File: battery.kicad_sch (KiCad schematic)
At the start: 62 parts, among them J10 SOLAR, Q10 SI2308, Q11 CSD17577Q3A, Q7 CSD18512Q5B, Q8 CSD18512Q5B, Q9 SI2308, SW3 POWER/RESET, U8 BQ25798

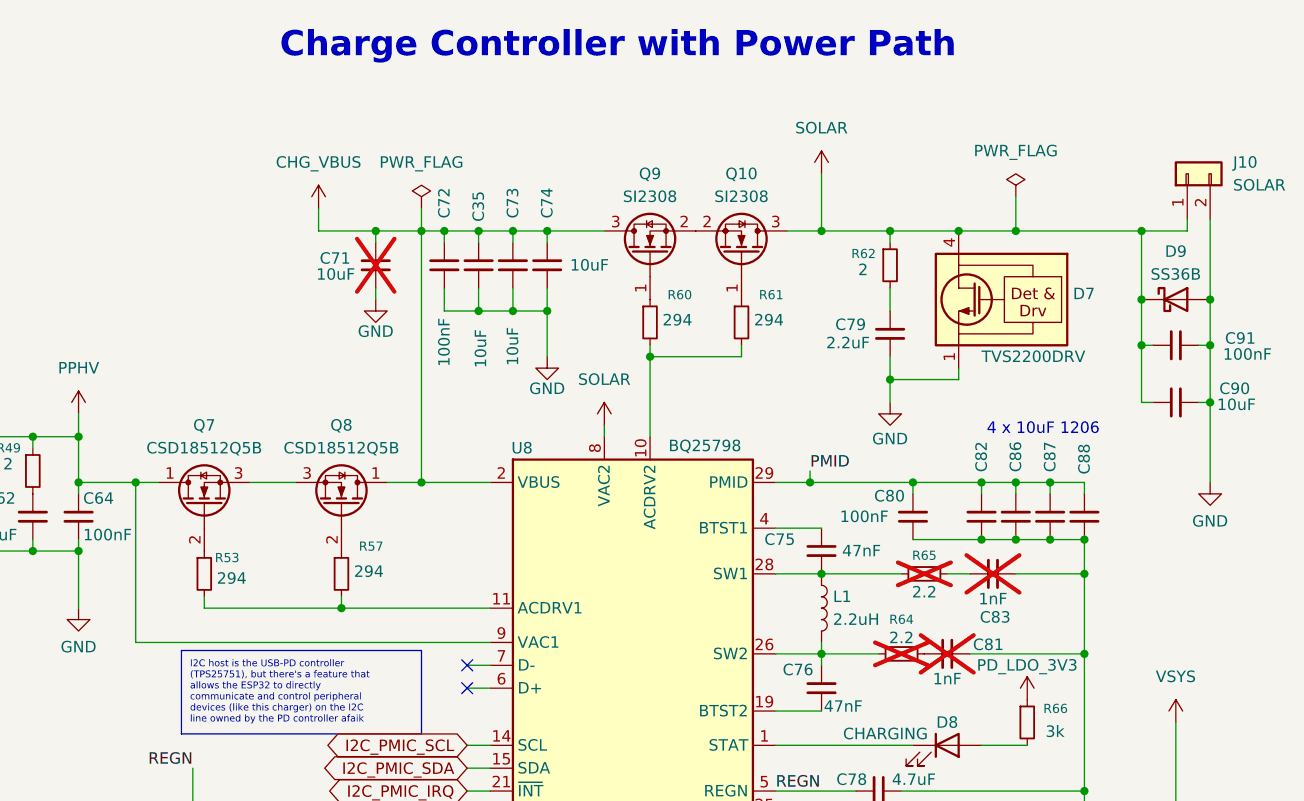
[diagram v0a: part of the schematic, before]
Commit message: schematic: add D24/D25 PZU12B2L zeners, Q_NMOS_SGD symbol, misc sheet edits
Co-Authored-By: Claude Opus 5.5 <noreply@anthropic.com>
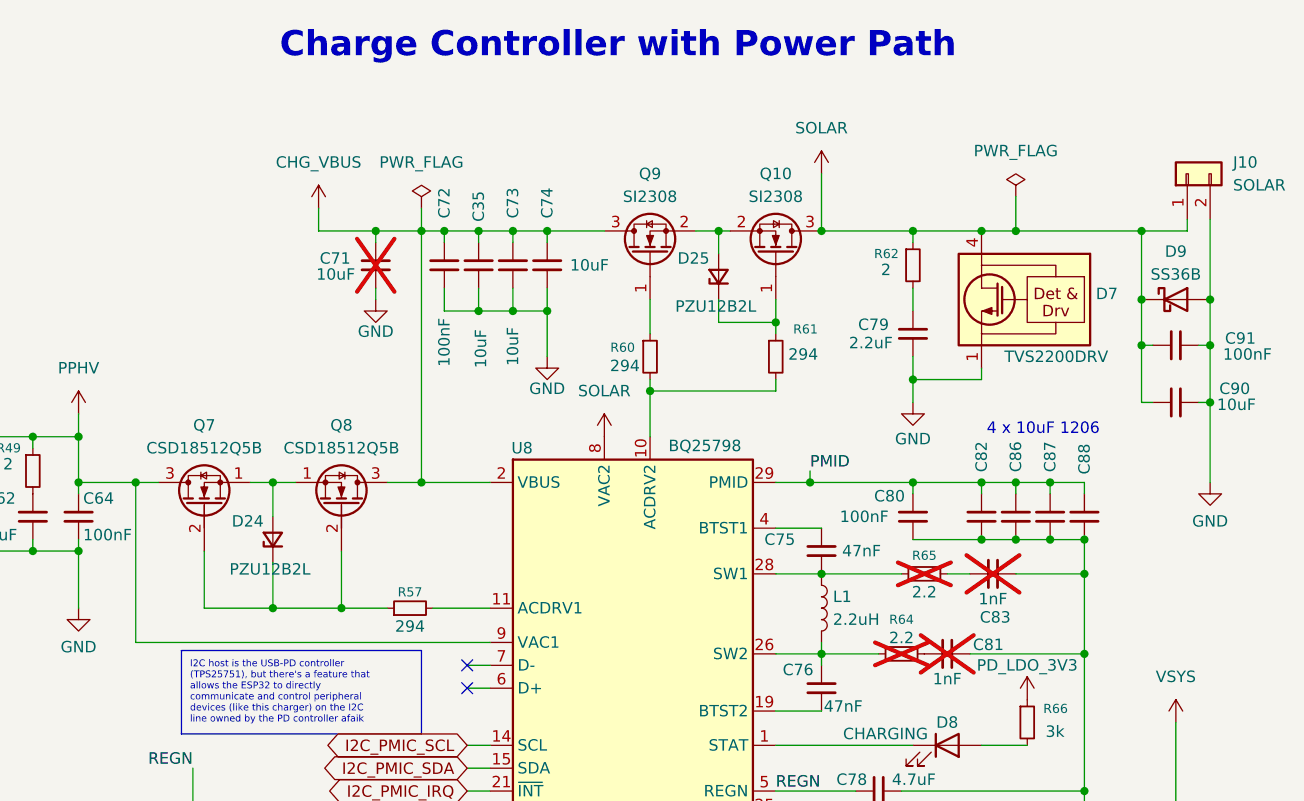
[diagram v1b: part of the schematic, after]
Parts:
- removed R53: 294, Resistor_SMD:R_0402_1005Metric, symbol Device:R_Small
- added D24, D25: PZU12B2L, Diode_SMD:D_SOD-882, symbol Device:D_Zener_Small
- Q7, Q8: symbol Transistor_FET:Q_NMOS_DGS -> Transistor_FET:Q_NMOS_SGD
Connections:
- net CHG_VBUS: now also Q8.3 (D); no longer Q8.1 (D)
- net PPHV: now also Q7.3 (D); no longer Q7.1 (D)
- net at Q8.2 (G), R57.1: now also Q7.2 (G), D24.1 (K)
- net at Q10.1 (G), R61.1: now also D25.1 (K)
- net at Q10.2 (S), Q9.2 (S): now also D25.2 (A)
- new net: D24.2 (A), Q7.1 (S), Q8.1 (S)
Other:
- moved on the sheet: C79, D7, Q10, R60, R61, R62

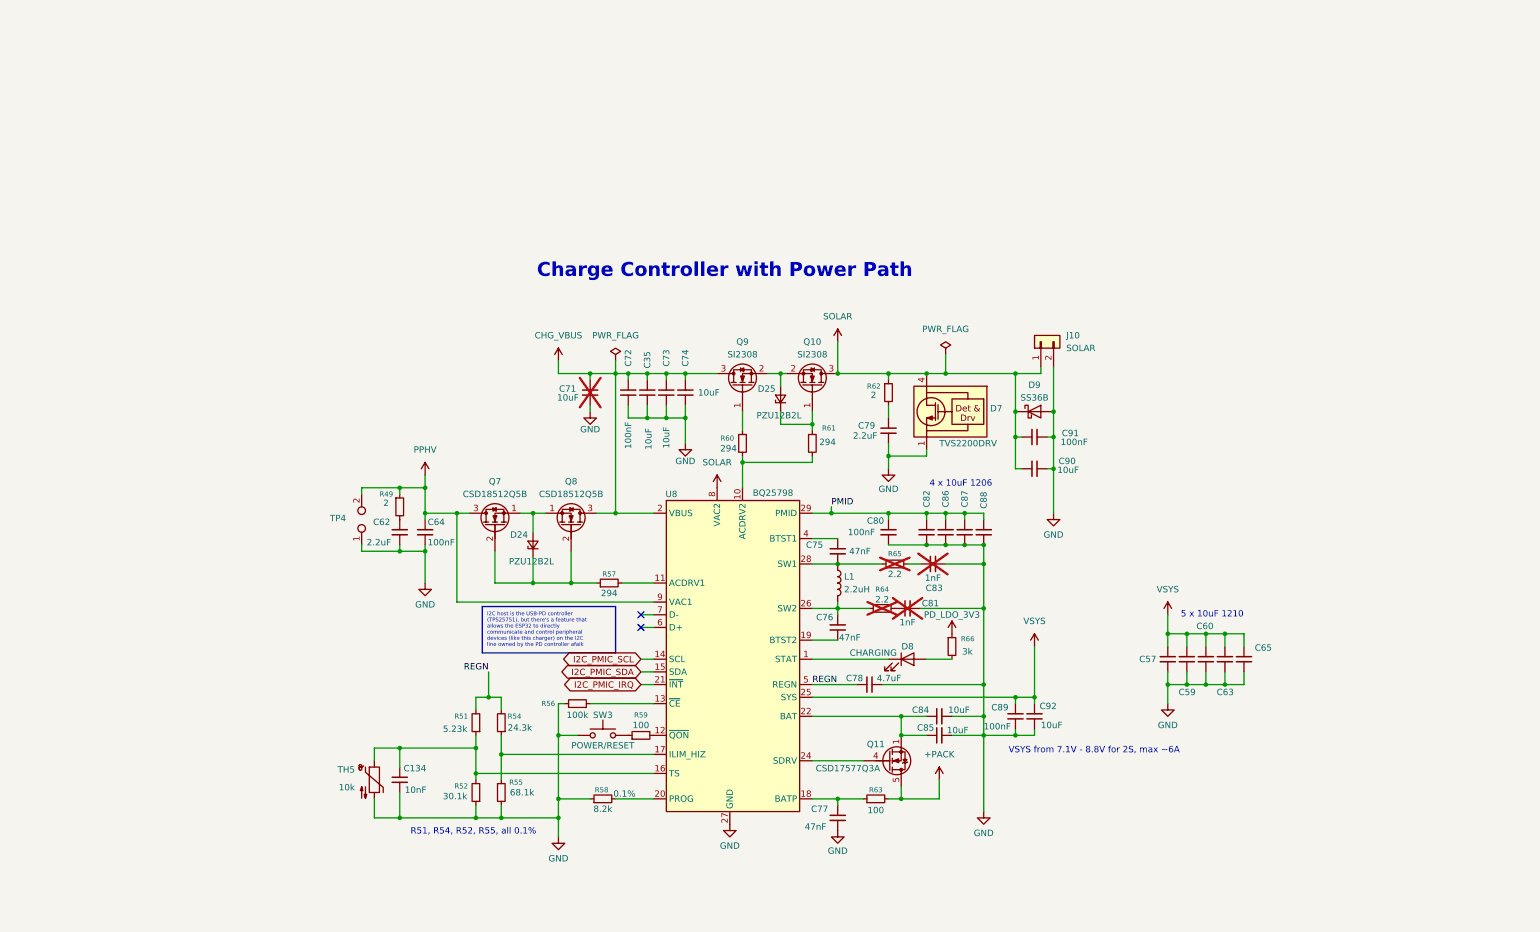
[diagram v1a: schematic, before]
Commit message: checkpoint: schematic WIP before battery -> charger rename
Connectors and Overview sheets, LSM6DSV16X/TPS22945/charger datasheets,
and in-progress edits across all sheets, committed as-is so the rename
diff stands alone.

Co-Authored-By: Claude Opus 5.5 <noreply@anthropic.com>
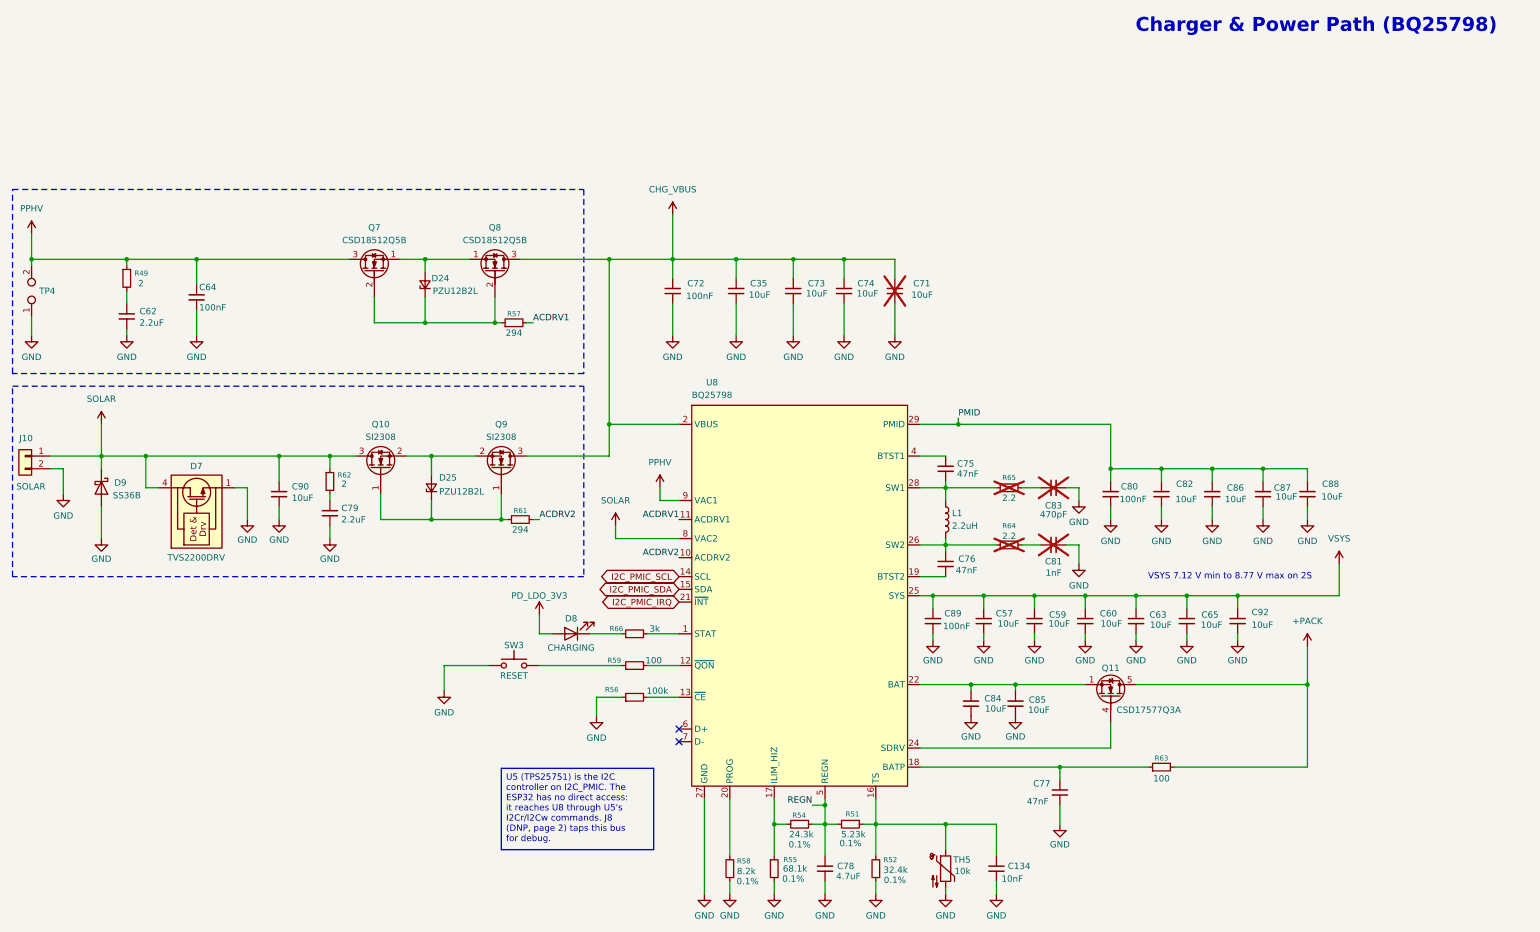
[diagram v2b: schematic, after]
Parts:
- removed C91: 100nF, Capacitor_SMD:C_0402_1005Metric, symbol Device:C_Small
- removed R60: 294, Resistor_SMD:R_0402_1005Metric, symbol Device:R_Small
- removed U8: BQ25798, Package_DFN_QFN:Texas_RQM0029A_VQFN-29_4x4mm_P0.4mm, symbol Battery_Management:BQ25798
- added U8: BQ25798, Package_DFN_QFN:Texas_RQM0029A_VQFN-29_4x4mm_P0.4mm, symbol parsnip-node:BQ25798
- C83: value 1nF -> 470pF
- L1: footprint Inductor_SMD:L_Sunlord_MWSA0503S -> Inductor_SMD:L_Sunlord_MWSA0603S; LCSC Part C408408 -> C357100; MPN MWSA0503S-2R2MT -> TMPA0603S-2R2MN-D
- R52: value 30.1k -> 32.4k; LCSC Part C2989442 -> C861323; MPN TC0325B3012T5F -> RT0603BRD0732K4L; Manufacturer UNI-ROYAL -> Yageo
- SW3: value POWER/RESET -> RESET
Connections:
- net CHG_VBUS: now also U8.2 (VBUS), U8.3 (VBUS)
- net GND: now also C78.1, C84.1, C85.1, C90.2, U8.27 (GND); no longer C78.2, C84.2, C85.2, C90.1
- net I2C_PMIC_IRQ: now also U8.21 (~{INT})
- net I2C_PMIC_SCL: now also U8.14 (SCL)
- net I2C_PMIC_SDA: now also U8.15 (SDA)
- net PD_LDO_3V3: now also D8.2 (A); no longer R66.1
- net PMID: now also U8.29 (PMID)
- net PPHV: now also U8.9 (VAC1)
- net REGN: now also C78.2, R54.1, U8.5 (REGN); no longer C78.1, R54.2
- net SOLAR: now also C90.1, U8.8 (VAC2); no longer C90.2
- net VSYS: now also U8.25 (SYS)
- net at C77.1, R63.1: now also U8.18 (BATP)
- net at D25.1 (K), Q10.1 (G), R61.1: now also Q9.1 (G)
- net at C76.1, L1.2, R64.1: now also U8.26 (SW2)
- net at R56.2: now also U8.13 (~{CE})
- net ACDRV2: now reaches R61.2
- net ACDRV2: now also U8.10 (ACDRV2)
- net at C134.1, R51.1, R52.2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: now also U8.16 (TS)
- net ACDRV1: now reaches R57.2
- net ACDRV1: now also U8.11 (ACDRV1)
- net at C76.2: now also U8.19 (BTST2)
- net at Q11.1 (S), Q11.2 (S), Q11.3 (S): now also C84.2, C85.2, U8.22 (BAT), U8.23 (BAT); no longer C84.1, C85.1
- net at R59.2: now also U8.12 (~{QON})
- net at R55.1: now also R54.2, U8.17 (ILIM_HIZ); no longer R54.1
- net at D8.1 (K): now also R66.1
- net at R58.2: now also U8.20 (PROG)
- net at Q11.4 (G): now also U8.24 (SDRV)
- net at C75.2, L1.1, R65.1: now also U8.28 (SW1)
- net at C75.1: now also U8.4 (BTST1)
- net at R66.2: now also U8.1 (STAT); no longer D8.2 (A)
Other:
- note added: "${TITLE}"
- note added: "VSYS 7.12 V min to 8.77 V max on 2S"
- note removed: "4 x 10uF 1206"
- note removed: "5 x 10uF 1210"
- note removed: "Charge Controller with Power Path"
- note removed: "R51, R54, R52, R55, all 0.1%"
- note removed: "VSYS from 7.1V - 8.8V for 2S, max ~6A"
- title: Battery Charge Controller -> Charger & Power Path (BQ25798)
